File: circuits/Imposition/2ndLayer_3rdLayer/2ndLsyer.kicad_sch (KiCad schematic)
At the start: 23 parts, among them J1 Conn_01x10_Pin, J2 Conn_02x10_Odd_Even, Q16 2N7002, SW1 SW_SPST, U8 STM32H723VGTx, Y1 16MHz

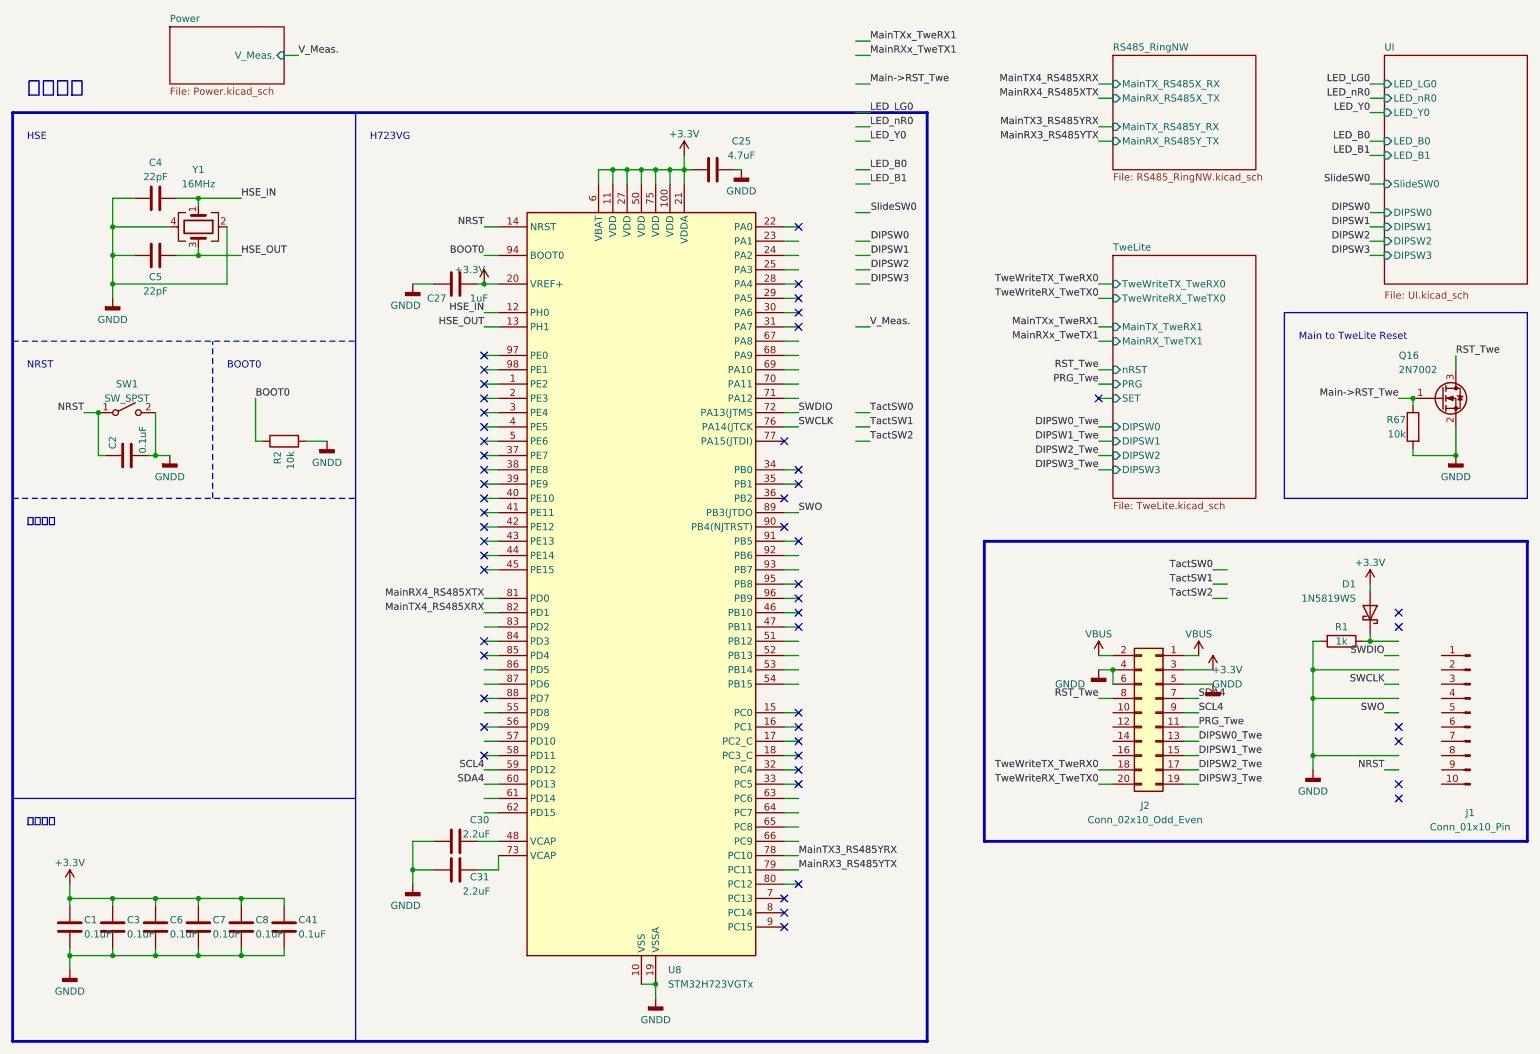
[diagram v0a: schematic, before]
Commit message: 発注_第一弾
Drive, 1stLayer_Power, 2ndLayer_3rdLayer
を発注
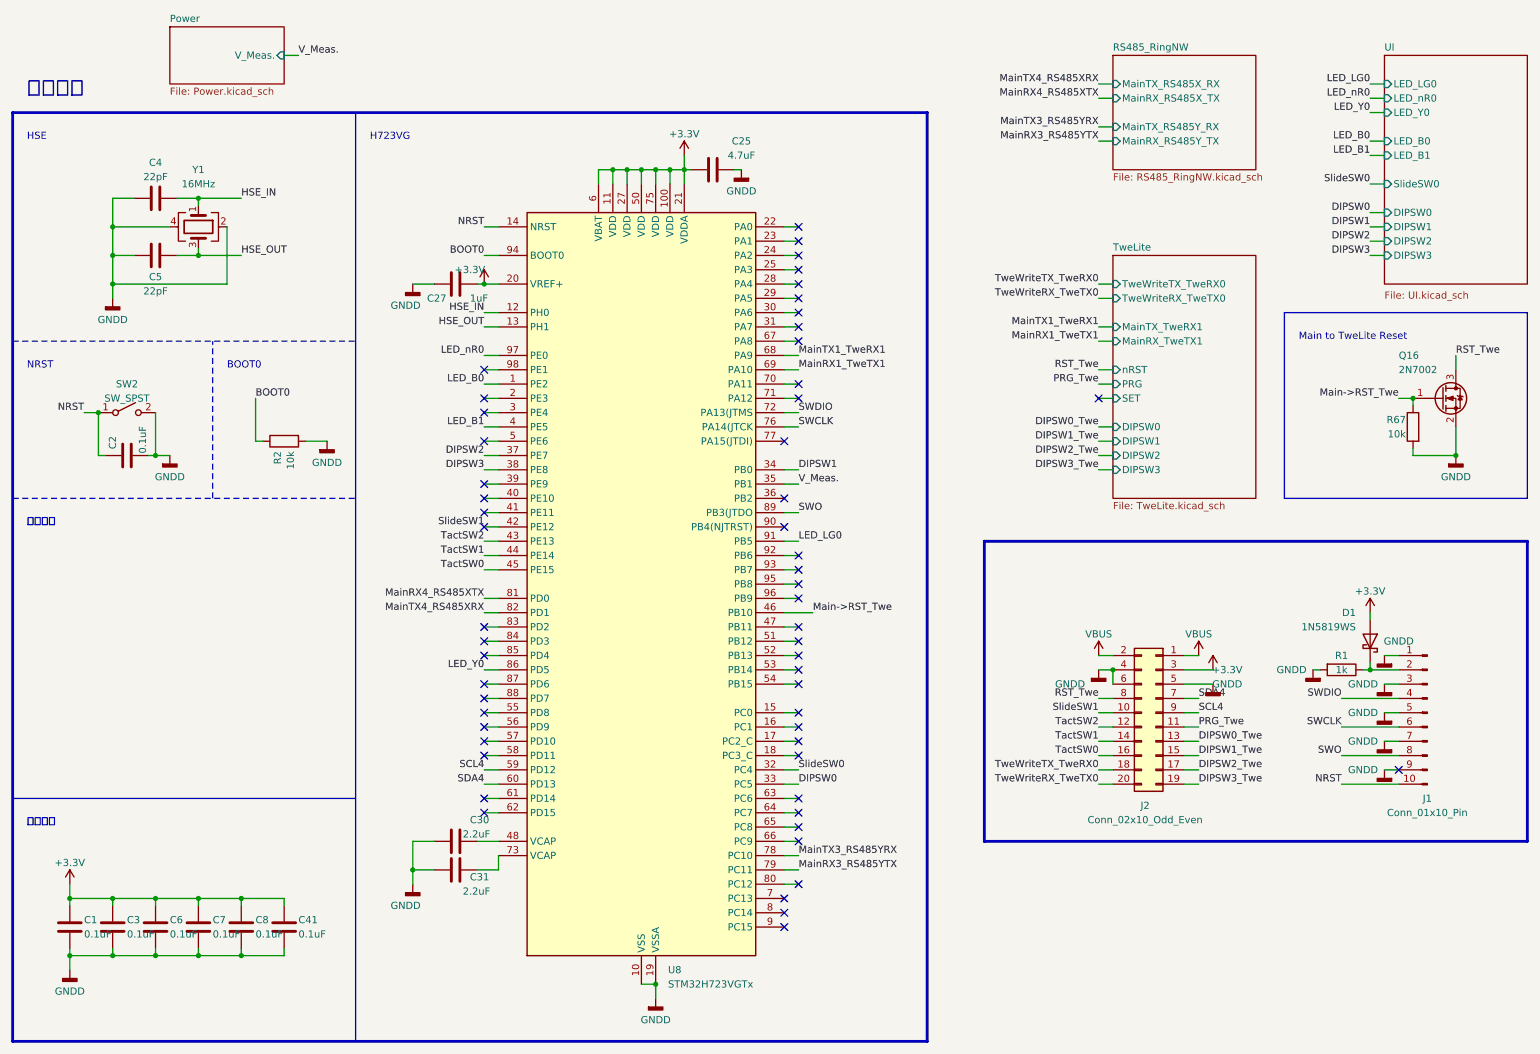
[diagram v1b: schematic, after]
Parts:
- renumbered SW1 to SW2
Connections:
- net DIPSW0: now also U8.33 (PC5)
- net DIPSW1: now also U8.34 (PB0)
- net DIPSW2: now also U8.37 (PE7)
- net DIPSW3: now also U8.38 (PE8)
- net GNDD: now also J1.1 (Pin_1), J1.3 (Pin_3), J1.5 (Pin_5), J1.7 (Pin_7), J1.9 (Pin_9)
- net LED_B0: now also U8.1 (PE2)
- net LED_B1: now also U8.4 (PE5)
- net LED_LG0: now also U8.91 (PB5)
- net LED_Y0: now also U8.86 (PD5)
- net LED_nR0: now also U8.97 (PE0)
- net Main->RST_Twe: now also U8.46 (PB10)
- net NRST: now also J1.10 (Pin_10)
- net SWCLK: now also J1.6 (Pin_6)
- net SWDIO: now also J1.4 (Pin_4)
- net SWO: now also J1.8 (Pin_8)
- net SlideSW0: now also U8.32 (PC4)
- net TactSW0: now also J2.16 (Pin_16), U8.45 (PE15)
- net TactSW1: now also J2.14 (Pin_14), U8.44 (PE14)
- net TactSW2: now also J2.12 (Pin_12), U8.43 (PE13)
- net V_Meas.: now also U8.35 (PB1)
- net SlideSW1: now reaches U8.42 (PE12)
- net SlideSW1: now also J2.10 (Pin_10)
- net MainTX1_TweRX1: now reaches U8.68 (PA9)
- net MainRX1_TweTX1: now reaches U8.69 (PA10)
- net at J1.2 (Pin_2): now also D1.1 (K), R1.1
- no-connect marks 53 -> 56
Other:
- moved on the sheet: D1, J1, R1
